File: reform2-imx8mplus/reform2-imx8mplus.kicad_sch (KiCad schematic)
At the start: 8 parts, among them J1 Conn_01x33, U1 reform2-som-connector, U2 Nit8M_Plus_SOM_J5, U3 Nit8M_Plus_SOM_J4, U4 Nit8M_Plus_SOM_J8

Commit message: imx8mplus: first rev routed
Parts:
- added C1: 1uF, Capacitor_SMD:C_0603_1608Metric, symbol Device:C_Small
- added R3: 1k, Capacitor_SMD:C_0603_1608Metric, symbol Device:R_Small
- added R4: 0, Capacitor_SMD:C_0603_1608Metric, symbol Device:R_Small
- added SW1: SW_SPST, Connector_PinHeader_2.00mm:PinHeader_1x02_P2.00mm_Horizontal, symbol Switch:SW_SPST
- added TP1: TP_USB1_ID, TestPoint:TestPoint_Pad_1.0x1.0mm, symbol Connector:TestPoint
- added TP2: TP_USB2_ID, TestPoint:TestPoint_Pad_1.0x1.0mm, symbol Connector:TestPoint
- added TP3: TP_ONOFF, TestPoint:TestPoint_Pad_1.0x1.0mm, symbol Connector:TestPoint
- added TP4: TP_ONREQ, TestPoint:TestPoint_Pad_1.0x1.0mm, symbol Connector:TestPoint
- added U5: NCP718xSN330, Package_TO_SOT_SMD:SOT-23-5, symbol Regulator_Linear:NCP718xSN330
- J2: renamed from J?; footprint (none) -> Connector_PinHeader_2.00mm:PinHeader_1x06_P2.00mm_Vertical
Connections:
- net +5V: now also C1.1, U5.1 (IN), U5.3 (EN)
- net BOOT_MODE1: now also SW1.2 (B); no longer U1.134 (SAI1_TXD2)
- net GND: now also C1.2, U5.2 (GND)
- net SD2_CD: now also R4.1; no longer U3.97 (GPIO1_IO05)
- net at U4.33 (PMIC_ON_REQ): now also TP4.1
- net at U4.35 (ONOFF): now also TP3.1
- net CLKIN1: now reaches U4.45 (CLKIN1)
- net at U4.46 (SD1_STROBE): now also R4.2
- net SD2_RESET: now reaches U4.48 (SD1_RESET_B)
- net CLKOUT1: now reaches U4.49 (CLKOUT1)
- net CLKIN2: now reaches U4.53 (CLKIN2)
- net CLKOUT2: now reaches U4.57 (CLKOUT2)
- net SD2_DATA4: now reaches U4.68 (SD1_DATA4)
- net SD2_DATA5: now reaches U4.70 (SD1_DATA5)
- net SD2_DATA6: now reaches U4.72 (SD1_DATA6)
- net SD2_DATA7: now reaches U4.74 (SD1_DATA7)
- net USB1_VBUS_3V3: now reaches U3.64 (USB1_VBUS_3V3)
- net USB1_VBUS_3V3: now also U3.69 (USB2_VBUS_3V3), R3.2, SW1.1 (A)
- net at U3.66 (USB1_ID): now also TP1.1
- net at U3.71 (USB2_ID): now also TP2.1
- net GPIO1_IO12: now reaches U3.87 (GPIO1_IO12)
- net GPIO1_IO09: now reaches U3.90 (GPIO1_IO09)
- net GPIO1_IO14: now reaches U3.93 (GPIO1_IO14)
- new net +3V3: R3.1, U5.5 (OUT)
- new net GPIO1_IO05: U3.97 (GPIO1_IO05)
- no-connect marks 181 -> 184
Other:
- note added: "TODO for MREF: pcie switch PI7C9X2G304SV"
- note added: "imx gpios"
- note removed: "TODO: check"

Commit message: imx8mplus: moved some things around; final tweaks and export for first test order
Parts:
- added GFX1: Logo, footprints:mntreform, symbol Mechanical:MountingHole
- added GFX2: Badge, footprints:reform2-imx8mplus-badge, symbol Mechanical:MountingHole
- added H1, H2, H3: MountingHole_Pad, MountingHole:MountingHole_2.2mm_M2_DIN965_Pad, symbol Mechanical:MountingHole_Pad
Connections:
- net GND: now also H1.1, H2.1, H3.1
- no-connect marks 184 -> 203

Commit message: imx8mplus: correct the mezzanine footprint, reroute everything, d-2 off to fab
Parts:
- added R5, R6: 0, Resistor_SMD:R_0603_1608Metric, symbol Device:R_Small
- added TP5: TP_5V, TestPoint:TestPoint_Pad_1.0x1.0mm, symbol Connector:TestPoint
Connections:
- net +5V: now also TP5.1
- net GND: no longer U1.123 (GND), U1.129 (GND)
- net USB1_N: now also R5.2; no longer U1.100 (USB1_D_N)
- net USB1_P: now also R6.2; no longer U1.102 (USB1_D_P)
- new net: R5.1, U1.100 (USB1_D_N)
- new net: R6.1, U1.102 (USB1_D_P)
- no-connect marks 203 -> 205
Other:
- note added: "??????"
- note added: "J4 on SOM, J8 on ENC"
- note added: "J5 on SOM, J2 on ENC"
- note added: "J8 on SOM, J33 on ENC"
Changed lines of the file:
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@@
   (junction (at 54.61 106.68) (diameter 0) (color 0 0 0 0)
   )
-  (junction (at 54.61 203.2) (diameter 0) (color 0 0 0 0)
-  )
   (junction (at 54.61 195.58) (diameter 0) (color 0 0 0 0)
   )
@@
   (junction (at 144.78 170.18) (diameter 0) (color 0 0 0 0)
   )
-  (junction (at 54.61 210.82) (diameter 0) (color 0 0 0 0)
-  )
   (junction (at 144.78 109.22) (diameter 0) (color 0 0 0 0)
   )
@@
   (no_connect (at 121.92 233.68))
   (no_connect (at 78.74 220.98))
+  (no_connect (at 78.74 203.2))
   (no_connect (at 459.74 184.15))
   (no_connect (at 78.74 116.84))
@@
   (no_connect (at 121.92 238.76))
   (no_connect (at 459.74 181.61))
+  (no_connect (at 78.74 210.82))
   (no_connect (at 78.74 93.98))
   (no_connect (at 198.12 269.24))
@@
     (stroke (width 0) (type default) (color 0 0 0 0))
   )
+  (wire (pts (xy 210.82 54.61) (xy 215.9 54.61))
+    (stroke (width 0) (type default) (color 0 0 0 0))
+  )
   (wire (pts (xy 279.4 241.3) (xy 254 241.3))
     (stroke (width 0) (type default) (color 0 0 0 0))
@@
     (stroke (width 0) (type default) (color 0 0 0 0))
   )
-  (wire (pts (xy 124.46 172.72) (xy 121.92 172.72))
+  (wire (pts (xy 121.92 172.72) (xy 148.59 172.72))
     (stroke (width 0) (type default) (color 0 0 0 0))
   )
@@
     (stroke (width 0) (type default) (color 0 0 0 0))
   )
-  (wire (pts (xy 54.61 251.46) (xy 54.61 210.82))
-    (stroke (width 0) (type default) (color 0 0 0 0))
-  )
   (wire (pts (xy 121.92 96.52) (xy 124.46 96.52))
     (stroke (width 0) (type default) (color 0 0 0 0))
@@
     (stroke (width 0) (type default) (color 0 0 0 0))
   )
-  (wire (pts (xy 121.92 175.26) (xy 124.46 175.26))
+  (wire (pts (xy 121.92 175.26) (xy 148.59 175.26))
     (stroke (width 0) (type default) (color 0 0 0 0))
   )
@@
     (stroke (width 0) (type default) (color 0 0 0 0))
   )
+  (wire (pts (xy 153.67 172.72) (xy 154.94 172.72))
+    (stroke (width 0) (type default) (color 0 0 0 0))
+  )
   (wire (pts (xy 267.97 157.48) (xy 267.97 154.94))
     (stroke (width 0) (type default) (color 0 0 0 0))
@@
     (stroke (width 0) (type default) (color 0 0 0 0))
   )
+  (wire (pts (xy 153.67 175.26) (xy 154.94 175.26))
+    (stroke (width 0) (type default) (color 0 0 0 0))
+  )
   (wire (pts (xy 76.2 226.06) (xy 78.74 226.06))
     (stroke (width 0) (type default) (color 0 0 0 0))
@@
     (stroke (width 0) (type default) (color 0 0 0 0))
   )
-  (wire (pts (xy 54.61 195.58) (xy 54.61 203.2))
-    (stroke (width 0) (type default) (color 0 0 0 0))
-  )
   (wire (pts (xy 124.46 119.38) (xy 121.92 119.38))
     (stroke (width 0) (type default) (color 0 0 0 0))
@@
     (stroke (width 0) (type default) (color 0 0 0 0))
   )
-  (wire (pts (xy 54.61 203.2) (xy 54.61 210.82))
+  (wire (pts (xy 54.61 195.58) (xy 54.61 251.46))
     (stroke (width 0) (type default) (color 0 0 0 0))
   )
@@
     (stroke (width 0) (type default) (color 0 0 0 0))
   )
-  (wire (pts (xy 54.61 210.82) (xy 78.74 210.82))
-    (stroke (width 0) (type default) (color 0 0 0 0))
-  )
   (wire (pts (xy 434.34 201.93) (xy 459.74 201.93))
     (stroke (width 0) (type default) (color 0 0 0 0))
@@
     (stroke (width 0) (type default) (color 0 0 0 0))
   )
-  (wire (pts (xy 78.74 203.2) (xy 54.61 203.2))
-    (stroke (width 0) (type default) (color 0 0 0 0))
-  )
   (wire (pts (xy 541.02 222.25) (xy 541.02 227.33))
     (stroke (width 0) (type default) (color 0 0 0 0))
@@
     (stroke (width 0) (type default) (color 0 0 0 0))
   )
+  (text "J4 on SOM, J8 on ENC" (at 340.36 135.89 0)
+    (effects (font (size 1.27 1.27)) (justify left bottom))
+  )
   (text "3v3 pulls on MB" (at 49.53 177.165 0)
     (effects (font (size 1.27 1.27)) (justify left bottom))
@@
     (effects (font (size 1.27 1.27)) (justify left bottom))
   )
+  (text "J8 on SOM, J33 on ENC" (at 477.52 137.16 0)
+    (effects (font (size 1.27 1.27)) (justify left bottom))
+  )
+  (text "??????" (at 311.15 151.13 0)
+    (effects (font (size 1.27 1.27)) (justify left bottom))
+  )
   (text "TODO" (at 415.29 195.58 0)
     (effects (font (size 1.27 1.27)) (justify left bottom))
   )
+  (text "??????" (at 382.27 151.13 0)
+    (effects (font (size 1.27 1.27)) (justify left bottom))
+  )
+  (text "J5 on SOM, J2 on ENC" (at 213.36 135.89 0)
+    (effects (font (size 1.27 1.27)) (justify left bottom))
+  )
   (text "TODO for MREF:\npcie switch\nPI7C9X2G304SV" (at 351.79 337.82 0)
     (effects (font (size 1.27 1.27)) (justify left bottom))
@@
     )
   )
-  (global_label "USB1_N" (shape bidirectional) (at 124.46 172.72 0) (fields_autoplaced)
+  (global_label "USB1_N" (shape bidirectional) (at 154.94 172.72 0) (fields_autoplaced)
     (effects (font (size 1.27 1.27)) (justify left))
-    (property "Intersheet References" "${INTERSHEET_REFS}" (id 0) (at 34.29 25.4 0)
+    (property "Intersheet References" "${INTERSHEET_REFS}" (id 0) (at 64.77 25.4 0)
       (effects (font (size 1.27 1.27)) hide)
     )
@@
     )
   )
-  (global_label "USB1_P" (shape bidirectional) (at 124.46 175.26 0) (fields_autoplaced)
+  (global_label "USB1_P" (shape bidirectional) (at 154.94 175.26 0) (fields_autoplaced)
     (effects (font (size 1.27 1.27)) (justify left))
-    (property "Intersheet References" "${INTERSHEET_REFS}" (id 0) (at 34.29 25.4 0)
+    (property "Intersheet References" "${INTERSHEET_REFS}" (id 0) (at 64.77 25.4 0)
       (effects (font (size 1.27 1.27)) hide)
     )
@@
     (pin "1")
   )
+  (symbol (lib_id "Device:R_Small") (at 151.13 172.72 90) (unit 1)
+    (in_bom yes) (on_board yes)
+    (property "Reference" "R5" (id 0) (at 151.13 170.18 90))
+    (property "Value" "0" (id 1) (at 153.67 170.18 90))
+    (property "Footprint" "Resistor_SMD:R_0603_1608Metric" (id 2) (at 151.13 172.72 0)
+      (effects (font (size 1.27 1.27)) hide)
+    )
+    (property "Datasheet" "~" (id 3) (at 151.13 172.72 0)
+      (effects (font (size 1.27 1.27)) hide)
+    )
+    (pin "1")
+    (pin "2")
+  )
   (symbol (lib_id "Device:R_Small") (at 518.16 270.51 90) (unit 1)
     (in_bom yes) (on_board yes)
@@
     (pin "2")
   )
+  (symbol (lib_id "Device:R_Small") (at 151.13 175.26 90) (unit 1)
+    (in_bom yes) (on_board yes)
+    (property "Reference" "R6" (id 0) (at 151.13 177.8 90))
+    (property "Value" "0" (id 1) (at 153.67 177.8 90))
+    (property "Footprint" "Resistor_SMD:R_0603_1608Metric" (id 2) (at 151.13 175.26 0)
+      (effects (font (size 1.27 1.27)) hide)
+    )
+    (property "Datasheet" "~" (id 3) (at 151.13 175.26 0)
+      (effects (font (size 1.27 1.27)) hide)
+    )
+    (pin "1")
+    (pin "2")
+  )
   (symbol (lib_id "power:+5V") (at 63.5 45.72 0) (unit 1)
     (in_bom yes) (on_board yes)
@@
     (pin "99")
   )
+  (symbol (lib_id "Connector:TestPoint") (at 210.82 54.61 90) (unit 1)
+    (in_bom yes) (on_board yes) (fields_autoplaced)
+    (property "Reference" "TP5" (id 0) (at 207.518 48.26 90))
+    (property "Value" "TP_5V" (id 1) (at 207.518 50.8 90))
+    (property "Footprint" "TestPoint:TestPoint_Pad_1.0x1.0mm" (id 2) (at 210.82 49.53 0)
+      (effects (font (size 1.27 1.27)) hide)
+    )
+    (property "Datasheet" "~" (id 3) (at 210.82 49.53 0)
+      (effects (font (size 1.27 1.27)) hide)
+    )
+    (pin "1")
+  )
   (symbol (lib_id "power:GND") (at 541.02 280.67 0) (unit 1)
     (in_bom yes) (on_board yes) (fields_autoplaced)
@@
       (reference "R4") (unit 1) (value "0") (footprint "Capacitor_SMD:C_0603_1608Metric")
     )
+    (path "/6be57e8b-2073-49d4-87e3-7ede2aeb4b69"
+      (reference "R5") (unit 1) (value "0") (footprint "Resistor_SMD:R_0603_1608Metric")
+    )
+    (path "/783d7a2b-8f7f-4a6c-b258-13ec50193c64"
+      (reference "R6") (unit 1) (value "0") (footprint "Resistor_SMD:R_0603_1608Metric")
+    )
     (path "/fcbe1c01-7b70-4e87-a73c-fd749a6cb51e"
       (reference "SW1") (unit 1) (value "SW_SPST") (footprint "Connector_PinHeader_2.00mm:PinHeader_1x02_P2.00mm_Horizontal")
@@
       (reference "TP4") (unit 1) (value "TP_ONREQ") (footprint "TestPoint:TestPoint_Pad_1.0x1.0mm")
     )
+    (path "/9afbc47c-1299-4741-bbf8-4e59e13f885c"
+      (reference "TP5") (unit 1) (value "TP_5V") (footprint "TestPoint:TestPoint_Pad_1.0x1.0mm")
+    )
     (path "/b4a40e00-b86f-4113-b137-cf35a6d41870"

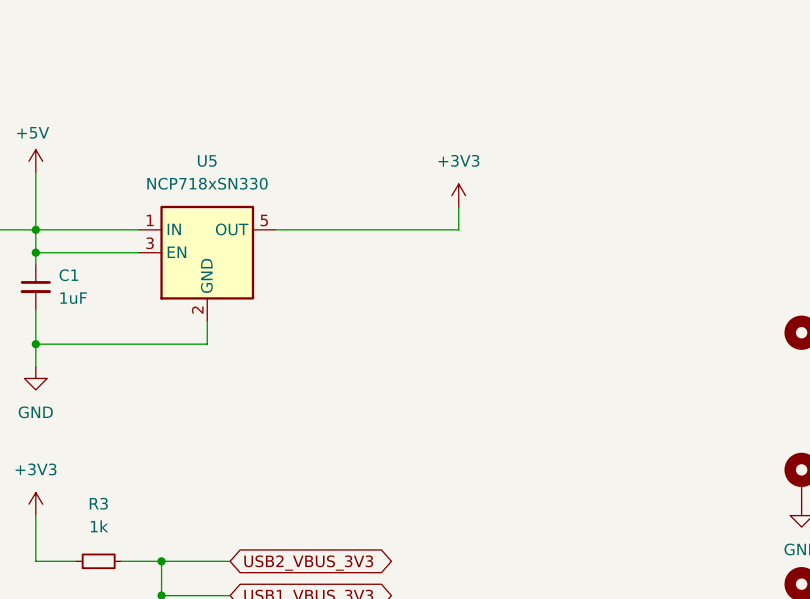
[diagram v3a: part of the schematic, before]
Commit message: imx8mplus: change drill size to 0.2mm, add optional 3v3 source via reset pin
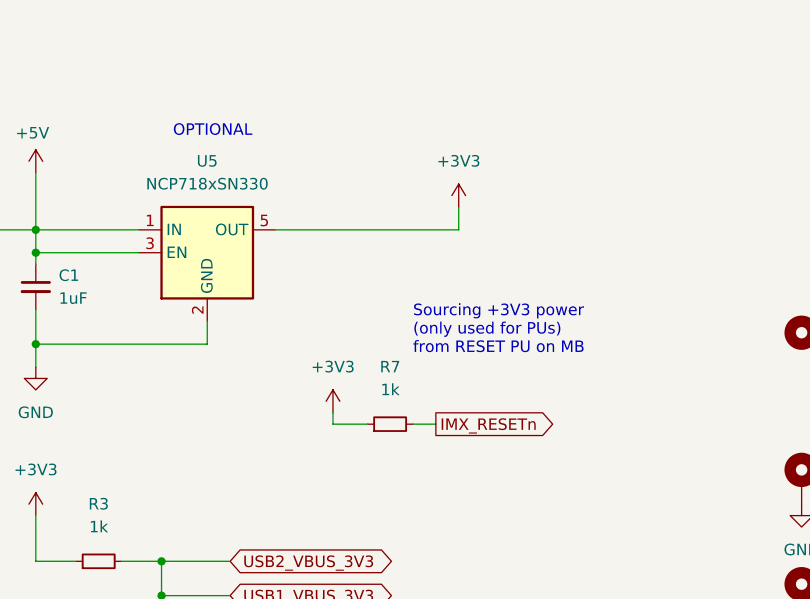
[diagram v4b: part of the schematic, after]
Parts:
- added R7: 1k, Capacitor_SMD:C_0603_1608Metric, symbol Device:R_Small
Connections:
- net +3V3: now also R7.1
- net IMX_RESETn: now also R7.2
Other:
- note added: "OPTIONAL"
- note added: "Sourcing +3V3 power (only used for PUs) from RESET PU on MB"
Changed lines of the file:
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@@
     (stroke (width 0) (type default) (color 0 0 0 0))
   )
+  (wire (pts (xy 248.92 76.2) (xy 252.73 76.2))
+    (stroke (width 0) (type default) (color 0 0 0 0))
+  )
   (wire (pts (xy 487.68 60.96) (xy 491.49 60.96))
     (stroke (width 0) (type default) (color 0 0 0 0))
@@
     (stroke (width 0) (type default) (color 0 0 0 0))
   )
+  (wire (pts (xy 248.92 74.93) (xy 248.92 76.2))
+    (stroke (width 0) (type default) (color 0 0 0 0))
+  )
   (wire (pts (xy 121.92 172.72) (xy 148.59 172.72))
     (stroke (width 0) (type default) (color 0 0 0 0))
@@
     (stroke (width 0) (type default) (color 0 0 0 0))
   )
+  (wire (pts (xy 257.81 76.2) (xy 260.35 76.2))
+    (stroke (width 0) (type default) (color 0 0 0 0))
+  )
   (wire (pts (xy 76.2 185.42) (xy 78.74 185.42))
     (stroke (width 0) (type default) (color 0 0 0 0))
@@
     (effects (font (size 1.27 1.27)) (justify left bottom))
   )
+  (text "OPTIONAL" (at 231.14 44.45 0)
+    (effects (font (size 1.27 1.27)) (justify left bottom))
+  )
   (text "imx gpios" (at 354.965 289.56 0)
     (effects (font (size 1.27 1.27)) (justify left bottom))
@@
     (effects (font (size 1.27 1.27)) (justify left bottom))
   )
+  (text "Sourcing +3V3 power\n(only used for PUs)\nfrom RESET PU on MB\n"
+    (at 257.81 68.58 0)
+    (effects (font (size 1.27 1.27)) (justify left bottom))
+  )
   (text "TODO for MREF:\npcie switch\nPI7C9X2G304SV" (at 351.79 337.82 0)
     (effects (font (size 1.27 1.27)) (justify left bottom))
@@
     )
   )
+  (global_label "IMX_RESETn" (shape output) (at 260.35 76.2 0) (fields_autoplaced)
+    (effects (font (size 1.27 1.27)) (justify left))
+    (property "Intersheet References" "${INTERSHEET_REFS}" (id 0) (at 302.26 208.28 0)
+      (effects (font (size 1.27 1.27)) hide)
+    )
+  )
   (global_label "SD2_CD" (shape input) (at 445.77 204.47 180) (fields_autoplaced)
     (effects (font (size 1.27 1.27)) (justify right))
@@
     (pin "2")
   )
+  (symbol (lib_id "Device:R_Small") (at 255.27 76.2 90) (unit 1)
+    (in_bom yes) (on_board yes) (fields_autoplaced)
+    (property "Reference" "R7" (id 0) (at 255.27 69.85 90))
+    (property "Value" "1k" (id 1) (at 255.27 72.39 90))
+    (property "Footprint" "Capacitor_SMD:C_0603_1608Metric" (id 2) (at 255.27 76.2 0)
+      (effects (font (size 1.27 1.27)) hide)
+    )
+    (property "Datasheet" "~" (id 3) (at 255.27 76.2 0)
+      (effects (font (size 1.27 1.27)) hide)
+    )
+    (pin "1")
+    (pin "2")
+  )
   (symbol (lib_id "power:+5V") (at 137.16 45.72 0) (mirror y) (unit 1)
     (in_bom yes) (on_board yes)
@@
     (pin "1")
   )
+  (symbol (lib_id "power:+3V3") (at 248.92 74.93 0) (unit 1)
+    (in_bom yes) (on_board yes) (fields_autoplaced)
+    (property "Reference" "#PWR0104" (id 0) (at 248.92 78.74 0)
+      (effects (font (size 1.27 1.27)) hide)
+    )
+    (property "Value" "+3V3" (id 1) (at 248.92 69.85 0))
+    (property "Footprint" "" (id 2) (at 248.92 74.93 0)
+      (effects (font (size 1.27 1.27)) hide)
+    )
+    (property "Datasheet" "" (id 3) (at 248.92 74.93 0)
+      (effects (font (size 1.27 1.27)) hide)
+    )
+    (pin "1")
+  )
   (symbol (lib_id "power:+3V3") (at 215.9 86.36 0) (unit 1)
     (in_bom yes) (on_board yes) (fields_autoplaced)
@@
       (reference "#PWR0103") (unit 1) (value "GND") (footprint "")
     )
+    (path "/ea13eca5-36c1-40e1-8dfd-e8357c130a9c"
+      (reference "#PWR0104") (unit 1) (value "+3V3") (footprint "")
+    )
     (path "/e108fc83-2982-4038-9b5a-ef38b363d222"
       (reference "C1") (unit 1) (value "1uF") (footprint "Capacitor_SMD:C_0603_1608Metric")
@@
       (reference "R6") (unit 1) (value "0") (footprint "Resistor_SMD:R_0603_1608Metric")
     )
+    (path "/9000a311-076c-4f64-8cbd-f33a0114ecb1"
+      (reference "R7") (unit 1) (value "1k") (footprint "Capacitor_SMD:C_0603_1608Metric")
+    )
     (path "/fcbe1c01-7b70-4e87-a73c-fd749a6cb51e"
